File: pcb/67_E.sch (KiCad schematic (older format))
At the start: 135 parts, among them U1 ATmega32U4-AU, U2 SRV05-4, X1 Crystal_GND24_Small

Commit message: replace all switch footprints with hotswap equivalents and begin re-routing PCB
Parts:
- removed MX15, MX16, MX67: MX-NoLED, MX_Only:MXOnly-1U-NoLED, symbol MX_Alps_Hybrid:MX-NoLED
- removed MX32, MX66, MX68, MX70: MX-NoLED, MX_Only:MXOnly-1.5U-NoLED, symbol MX_Alps_Hybrid:MX-NoLED
- removed MX34: MX-LED, custom_parts:MXOnly-1.25U-flipped-LED, symbol MX_Alps_Hybrid:MX-LED
- removed MX48, MX51: MX-NoLED, MX_Only:MXOnly-2.25U-NoLED, symbol MX_Alps_Hybrid:MX-NoLED
- removed MX69: MX-NoLED, MX_Only:MXOnly-7U-ReversedStabilizers-NoLED, symbol MX_Alps_Hybrid:MX-NoLED
- removed R7: 1.5k, Resistor_SMD:R_0805_2012Metric, symbol Device:R_Small
- MX1: footprint MX_Only:MXOnly-2U-NoLED -> MX_Only:MXOnly-2U-Hotswap-LED
- MX10, MX11, MX12, MX13, MX14, MX17, MX18, MX2, MX20, MX21, MX22, MX23, MX24, MX25, MX26, MX27, MX28, MX29, MX3, MX30, MX31, MX33, MX37, MX38, MX39, MX4, MX40, MX41, MX42, MX43, MX44, MX45, MX46, MX47, MX49, MX5, MX52, MX53, MX54, MX55, MX56, MX57, MX58, MX59, MX6, MX60, MX61, MX62, MX64, MX65, MX7, MX77, MX78, MX79, MX8, MX9: footprint MX_Only:MXOnly-1U-NoLED -> MX_Only:MXOnly-1U-Hotswap
- MX19: footprint MX_Only:MXOnly-1.5U-NoLED -> MX_Only:MXOnly-1.5U-Hotswap
- MX35: footprint MX_Only:MXOnly-ISO-ReversedStabilizers-NoLED -> MX_Only:MXOnly-ISO-Hotswap-ReversedStabilizers
- MX36: footprint MX_Only:MXOnly-1.75U -> MX_Only:MXOnly-1.75U-Hotswap
- MX50, MX71, MX72, MX73, MX75, MX76: footprint MX_Only:MXOnly-1.25U-NoLED -> MX_Only:MXOnly-1.25U-Hotswap
- MX63: footprint MX_Only:MXOnly-1.75U-NoLED -> MX_Only:MXOnly-1.75U-Hotswap
- MX74: footprint MX_Only:MXOnly-6.25U-ReversedStabilizers-NoLED -> MX_Only:MXOnly-6.25U-Hotswap-ReversedStabilizers
- USB1: symbol Connector:USB_C_Receptacle_USB2.0 -> 67_E-rescue:USB_C_Receptacle_USB2.0-Connector
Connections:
- net labels removed: capsLED
- wire segments 273 -> 239

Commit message: remove unused LED footprint
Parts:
- MX1: footprint MX_Only:MXOnly-2U-Hotswap-LED -> MX_Only:MXOnly-2U-Hotswap
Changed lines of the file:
@@
 F 0 "MX1" V 12477 2566 60  0000 C CNN
 F 1 "MX-NoLED" V 12551 2566 20  0000 C CNN
-F 2 "MX_Only:MXOnly-2U-Hotswap-LED" H 12075 2575 60  0001 C CNN
+F 2 "MX_Only:MXOnly-2U-Hotswap" H 12075 2575 60  0001 C CNN
 F 3 "" H 12075 2575 60  0001 C CNN
 	1    12700 2600

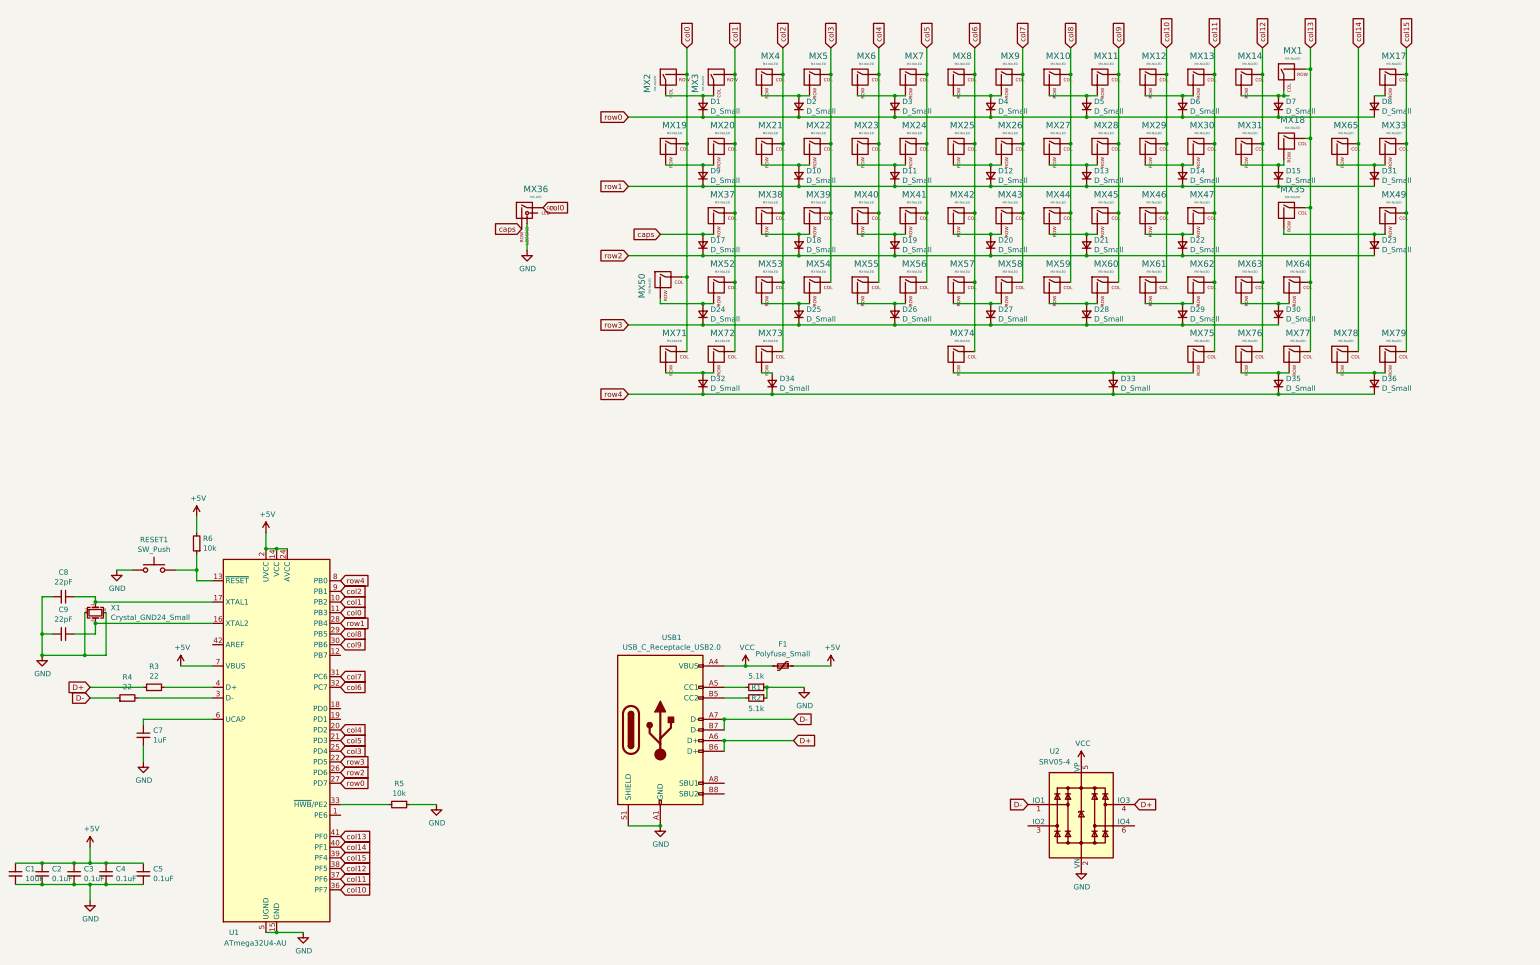
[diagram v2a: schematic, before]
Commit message: Add RGB underglow to PCB
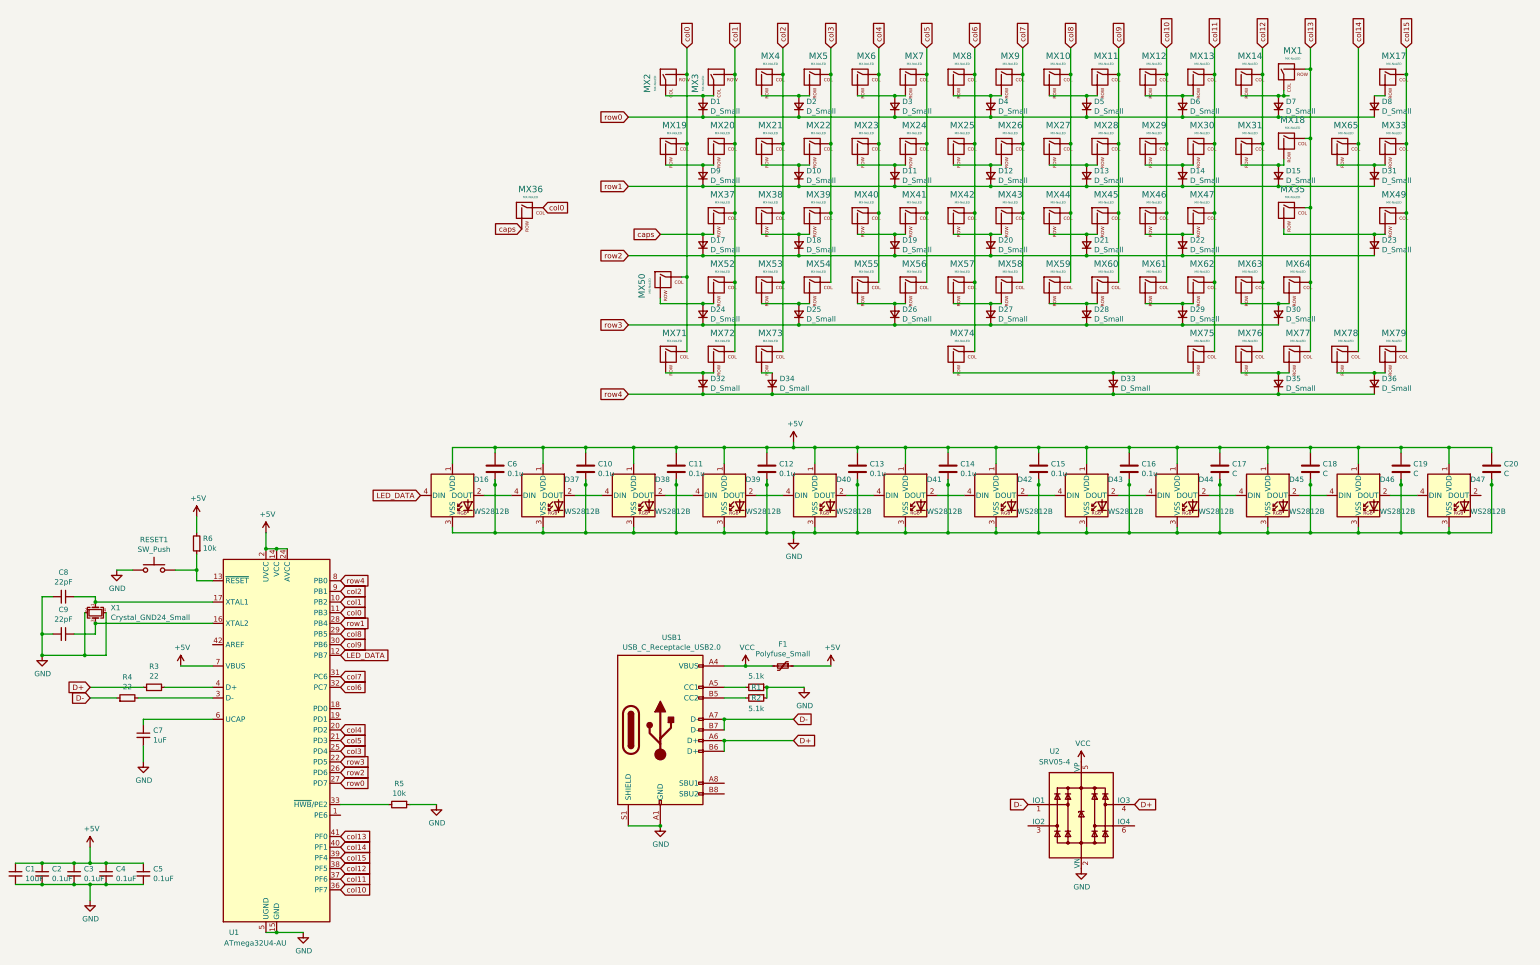
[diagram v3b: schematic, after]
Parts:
- removed MX36: MX-LED, MX_Only:MXOnly-1.75U-Hotswap, symbol MX_Alps_Hybrid:MX-LED
- added C10, C11, C12, C13, C14, C15, C16, C6: 0.1u, Capacitor_SMD:C_0805_2012Metric, symbol Device:C
- added C17, C18, C19, C20: C, Capacitor_SMD:C_0805_2012Metric, symbol Device:C
- added D16, D37, D38, D39, D40, D41, D42, D43, D44, D45, D46, D47: WS2812B, LED_SMD:LED_WS2812B_PLCC4_5.0x5.0mm_P3.2mm, symbol LED:WS2812B
- added MX36: MX-NoLED, MX_Only:MXOnly-1.75U-Hotswap, symbol MX_Alps_Hybrid:MX-NoLED
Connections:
- net labels added: LED_DATA
- wire segments 239 -> 359

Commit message: wip
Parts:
- C10, C11, C12, C13, C14, C15, C16, C6: value 0.1u -> 0.1uF
- C17, C18, C19, C20: value C -> 0.1uF
- RESET1: footprint Button_Switch_SMD:SW_SPST_TL3342 -> TestPoint:TestPoint_2Pads_Pitch2.54mm_Drill0.8mm
- X1: value Crystal_GND24_Small -> 16MHz
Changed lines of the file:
@@
 P 1500 7650
 F 0 "X1" V 1454 7794 50  0000 L CNN
-F 1 "Crystal_GND24_Small" V 1545 7794 50  0000 L CNN
+F 1 "16MHz" V 1545 7794 50  0000 L CNN
 F 2 "Crystal:Crystal_SMD_3225-4Pin_3.2x2.5mm" H 1500 7650 50  0001 C CNN
 F 3 "~" H 1500 7650 50  0001 C CNN
@@
 F 0 "RESET1" H 2050 7535 50  0000 C CNN
 F 1 "SW_Push" H 2050 7444 50  0000 C CNN
-F 2 "Button_Switch_SMD:SW_SPST_TL3342" H 2050 7450 50  0001 C CNN
+F 2 "TestPoint:TestPoint_2Pads_Pitch2.54mm_Drill0.8mm" H 2050 7450 50  0001 C CNN
 F 3 "~" H 2050 7450 50  0001 C CNN
 F 4 "C318884" H 2050 7250 50  0001 C CNN "LCSC"
@@
 P 5250 6300
 F 0 "C6" H 5365 6346 50  0000 L CNN
-F 1 "0.1u" H 5365 6255 50  0000 L CNN
+F 1 "0.1uF" H 5365 6255 50  0000 L CNN
 F 2 "Capacitor_SMD:C_0805_2012Metric" H 5288 6150 50  0001 C CNN
 F 3 "~" H 5250 6300 50  0001 C CNN
@@
 P 6100 6300
 F 0 "C10" H 6215 6346 50  0000 L CNN
-F 1 "0.1u" H 6215 6255 50  0000 L CNN
+F 1 "0.1uF" H 6215 6255 50  0000 L CNN
 F 2 "Capacitor_SMD:C_0805_2012Metric" H 6138 6150 50  0001 C CNN
 F 3 "~" H 6100 6300 50  0001 C CNN
@@
 P 6950 6300
 F 0 "C11" H 7065 6346 50  0000 L CNN
-F 1 "0.1u" H 7065 6255 50  0000 L CNN
+F 1 "0.1uF" H 7065 6255 50  0000 L CNN
 F 2 "Capacitor_SMD:C_0805_2012Metric" H 6988 6150 50  0001 C CNN
 F 3 "~" H 6950 6300 50  0001 C CNN
@@
 P 7800 6300
 F 0 "C12" H 7915 6346 50  0000 L CNN
-F 1 "0.1u" H 7915 6255 50  0000 L CNN
+F 1 "0.1uF" H 7915 6255 50  0000 L CNN
 F 2 "Capacitor_SMD:C_0805_2012Metric" H 7838 6150 50  0001 C CNN
 F 3 "~" H 7800 6300 50  0001 C CNN
@@
 P 8650 6300
 F 0 "C13" H 8765 6346 50  0000 L CNN
-F 1 "0.1u" H 8765 6255 50  0000 L CNN
+F 1 "0.1uF" H 8765 6255 50  0000 L CNN
 F 2 "Capacitor_SMD:C_0805_2012Metric" H 8688 6150 50  0001 C CNN
 F 3 "~" H 8650 6300 50  0001 C CNN
@@
 P 9500 6300
 F 0 "C14" H 9615 6346 50  0000 L CNN
-F 1 "0.1u" H 9615 6255 50  0000 L CNN
+F 1 "0.1uF" H 9615 6255 50  0000 L CNN
 F 2 "Capacitor_SMD:C_0805_2012Metric" H 9538 6150 50  0001 C CNN
 F 3 "~" H 9500 6300 50  0001 C CNN
@@
 P 10350 6300
 F 0 "C15" H 10465 6346 50  0000 L CNN
-F 1 "0.1u" H 10465 6255 50  0000 L CNN
+F 1 "0.1uF" H 10465 6255 50  0000 L CNN
 F 2 "Capacitor_SMD:C_0805_2012Metric" H 10388 6150 50  0001 C CNN
 F 3 "~" H 10350 6300 50  0001 C CNN
@@
 P 11200 6300
 F 0 "C16" H 11315 6346 50  0000 L CNN
-F 1 "0.1u" H 11315 6255 50  0000 L CNN
+F 1 "0.1uF" H 11315 6255 50  0000 L CNN
 F 2 "Capacitor_SMD:C_0805_2012Metric" H 11238 6150 50  0001 C CNN
 F 3 "~" H 11200 6300 50  0001 C CNN
@@
 P 12050 6300
 F 0 "C17" H 12165 6346 50  0000 L CNN
-F 1 "C" H 12165 6255 50  0000 L CNN
+F 1 "0.1uF" H 12165 6255 50  0000 L CNN
 F 2 "Capacitor_SMD:C_0805_2012Metric" H 12088 6150 50  0001 C CNN
 F 3 "~" H 12050 6300 50  0001 C CNN
@@
 P 12900 6300
 F 0 "C18" H 13015 6346 50  0000 L CNN
-F 1 "C" H 13015 6255 50  0000 L CNN
+F 1 "0.1uF" H 13015 6255 50  0000 L CNN
 F 2 "Capacitor_SMD:C_0805_2012Metric" H 12938 6150 50  0001 C CNN
 F 3 "~" H 12900 6300 50  0001 C CNN
@@
 P 13750 6300
 F 0 "C19" H 13865 6346 50  0000 L CNN
-F 1 "C" H 13865 6255 50  0000 L CNN
+F 1 "0.1uF" H 13865 6255 50  0000 L CNN
 F 2 "Capacitor_SMD:C_0805_2012Metric" H 13788 6150 50  0001 C CNN
 F 3 "~" H 13750 6300 50  0001 C CNN
@@
 P 14600 6300
 F 0 "C20" H 14715 6346 50  0000 L CNN
-F 1 "C" H 14715 6255 50  0000 L CNN
+F 1 "0.1uF" H 14715 6255 50  0000 L CNN
 F 2 "Capacitor_SMD:C_0805_2012Metric" H 14638 6150 50  0001 C CNN
 F 3 "~" H 14600 6300 50  0001 C CNN
